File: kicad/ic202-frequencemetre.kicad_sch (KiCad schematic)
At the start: 36 parts, among them J1 +12V IN, J2 RF IN, J3 DIV SEL, Q1 2N2369, U1 L7805, U2 LM317L, U3 MB506

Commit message: Modification 1 : rail 3 V et afficheur LCD TN au bout d'une nappe
La fiche docs/LCD.png montre un afficheur a cristaux liquides TN multiplexe
en 1/4 duty et 1/2 bias sous 3,0 V, et non un afficheur a LED. Consequences :

- rail regule ramene de 3,3 V a 3,0 V, R2 passe de 160 R a 140 R ;
- les 10 broches se repartissent en 4 communs et 6 segments ;
- les resistances de limitation disparaissent au profit d'une polarisation a
  mi-tension : R7..R16 de 100 k vers VLCD_MID, pont R17/R18 et decouplage C12.
  Une broche en haute impedance fournit ainsi le troisieme niveau ;
- J4 represente le connecteur de la nappe 10 conducteurs vers le LCD deporte.

L'ancien symbole 7SEG_3DIGIT_CC est remplace par LCD_3DIGIT_TN_10PIN. La
repartition COM/SEG sur les 10 broches reste une hypothese, signalee dans le
README et a confirmer avant fabrication.

ERC sans erreur ni avertissement, netlist verifiee broche a broche.

Co-Authored-By: Claude Opus 5 <noreply@anthropic.com>
Claude-Session: https://claude.ai/code/session_017jkpXZgM5sH1vt8JFfAijf
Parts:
- removed DS1: 3 digit CC, symbol IC202:7SEG_3DIGIT_CC
- added C12: 1u, Capacitor_SMD:C_0805_2012Metric, symbol Device:C
- added DS1: LCD 3 digits TN, symbol IC202:LCD_3DIGIT_TN_10PIN
- added J4: LCD, Connector_JST:JST_SH_SM10B-SRSS-TB_1x10-1MP_P1.00mm_Horizontal, symbol Connector_Generic:Conn_01x10
- added R17, R18: 10k, Resistor_SMD:R_0603_1608Metric, symbol Device:R
- R10, R11, R12, R13, R7, R8, R9: value 220R -> 100k
- R14, R15, R16: value 100R -> 100k
- R2: value 160R -> 140R
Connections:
- net GND: now also C12.2, R18.2
- net LCD_SEG2: now reaches R12.1
- net LCD_SEG2: now also A1.11 (D8), DS1.6 (SEG2), J4.6 (Pin_6)
- net VLCD_MID: now reaches R14.2
- net VLCD_MID: now also R10.2, R11.2, R12.2, R13.2, R15.2, R16.2, R7.2, R8.2, R9.2, C12.1, R17.2, R18.1
- net LCD_COM4: now reaches R10.1
- net LCD_COM4: now also A1.9 (D6), DS1.4 (COM4), J4.4 (Pin_4)
- net LCD_SEG3: now reaches R13.1
- net LCD_SEG3: now also A1.12 (D9), DS1.7 (SEG3), J4.7 (Pin_7)
- net LCD_COM3: now reaches R9.1
- net LCD_COM3: now also A1.7 (D4), DS1.3 (COM3), J4.3 (Pin_3)
- net LCD_SEG1: now reaches R11.1
- net LCD_SEG1: now also A1.10 (D7), DS1.5 (SEG1), J4.5 (Pin_5)
- net LCD_COM1: now reaches R7.1
- net LCD_COM1: now also A1.5 (D2), DS1.1 (COM1), J4.1 (Pin_1)
- net LCD_COM2: now reaches R8.1
- net LCD_COM2: now also A1.6 (D3), DS1.2 (COM2), J4.2 (Pin_2)
- net +3V3 renamed +3V
- net +3V: now also R17.1
- net D10 renamed LCD_SEG4
- net LCD_SEG4: now also DS1.8 (SEG4), J4.8 (Pin_8)
- net D11 renamed LCD_SEG5
- net LCD_SEG5: now also DS1.9 (SEG5), J4.9 (Pin_9)
- net D12 renamed LCD_SEG6
- net LCD_SEG6: now also DS1.10 (SEG6), J4.10 (Pin_10)
- removed net D2: A1.5 (D2), R7.2
- removed net D3: A1.6 (D3), R8.2
- removed net D4: A1.7 (D4), R9.2
- removed net D6: A1.9 (D6), R10.2
- removed net D7: A1.10 (D7), R11.2
- removed net D8: A1.11 (D8), R12.2
- removed net D9: A1.12 (D9), R13.2
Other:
- note added: "AFFICHEUR LCD 3 DIGITS TN (1/4 duty, 1/2 bias, 3V)"
- note added: "ALIMENTATION 12V -> 5V -> 3V"
- note added: "ARDUINO PRO MINI (alimente en 3V)"
- note added: "MISE EN FORME 3V -> D5"
- note added: "R17/R18/C12 : reference VLCD_MID = 3V/2. J4 : nappe 10 conducteurs vers le LCD deporte."
- note added: "R7..R16 : polarisation a mi-tension. Broche Arduino en haute impedance = 1,5 V, sinon 0 ou 3 V."
- note removed: "AFFICHEUR 3 DIGITS MULTIPLEXE (cathode commune)"
- note removed: "ALIMENTATION 12V -> 5V -> 3V3"
- note removed: "ARDUINO PRO MINI 3V3 / 8 MHz"
- note removed: "DS1 : numeros de broches a verifier sur la datasheet de l afficheur reel"
- note removed: "MISE EN FORME 3V3 -> D5"
- note removed: "R7..R13 -> segments A..G R14..R16 -> digits DIG1..DIG3"

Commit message: Modification 2 : corrections de valeurs d'apres le schema relu
docs/Schema_propre.jpg, une reprise nettement plus lisible du schema
manuscrit, a permis de corriger plusieurs valeurs mal lues sur la premiere
photo et de completer un composant manquant :

- R1 100R->220R, R2 160R->300R (diviseur du LM317L) ;
- R4 1k->3,3k (base de Q1), R6 1k->470R (collecteur de Q1) ;
- C8 1n->100n (decouplage de la broche ~IN du MB506) ;
- R17/R18 10k->3,3k chacune (pont de polarisation du LCD) ;
- ajout de R19 (2K2), pull-down manquant sur la sortie OUT du MB506,
  visible sur le schema relu et absent de la premiere transcription ;
- suppression de l'ancien R5 (100k base->GND) et du connecteur J3
  (selecteur SW1/SW2), absents du schema relu ; SW1/SW2 marquees non
  connectees, ce qui fixe le rapport de division a 1/256.

Le README documente le tableau des corrections et les deux points restes
ambigus : le brochage exact de U1 (78xx05) et un reseau optionnel visible
pres de la broche 8 du MB506 dont les deux extremites semblent en l'air
sur le dessin.

ERC : 0 erreur, 0 avertissement. Netlist et regles de lisibilite verifiees.

Co-Authored-By: Claude Sonnet 5 <noreply@anthropic.com>
Claude-Session: https://claude.ai/code/session_017jkpXZgM5sH1vt8JFfAijf
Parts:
- removed J3: DIV SEL, Connector_PinHeader_2.54mm:PinHeader_1x03_P2.54mm_Vertical, symbol Connector_Generic:Conn_01x03
- removed R5: 100k, Resistor_SMD:R_0603_1608Metric, symbol Device:R
- added R19: 2K2, Resistor_SMD:R_0603_1608Metric, symbol Device:R
- C8: value 1n -> 100n
- R1: value 100R -> 220R
- R17, R18: value 10k -> 3k3
- R2: value 140R -> 300R
- R4: value 1k -> 3k3
- R6: value 1k -> 470R
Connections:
- net GND: now also R19.2
- net at C10.1, U3.4 (OUT): now also R19.1
- net SW1: no longer names the net of U3.3 (SW1)
- net SW2: no longer names the net of U3.6 (SW2)
- no-connect marks 13 -> 15
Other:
- note added: "PREDIVISEUR MB506 (division fixe 1/256)"
- note added: "SW1/SW2 non connectes (ouverts) : division fixe par 256. Voir README pour reconfigurer."
- note removed: "J3 : SW1/SW2 ouverts = 1/256 ; relies a +5V = 1/64 (voir README)"
- note removed: "PREDIVISEUR MB506 (1/64 - 1/128 - 1/256 selon J3)"
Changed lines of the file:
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@@
 			)
 		)
-		(property "Value" "100R"
+		(property "Value" "220R"
 			(at 162.56 38.1 90)
 			(show_name no)
@@
 			)
 		)
-		(property "Value" "140R"
+		(property "Value" "300R"
 			(at 162.56 50.8 90)
 			(show_name no)
@@
 			)
 		)
-		(property "Value" "1n"
+		(property "Value" "100n"
 			(at 64.77 113.665 0)
 			(show_name no)
@@
 				)
 				(justify right)
+				(hide no)
 			)
 		)
@@
 	)
 	(symbol
-		(lib_id "Connector_Generic:Conn_01x03")
-		(at 55.88 132.08 180)
-		(unit 1)
-		(body_style 1)
-		(exclude_from_sim no)
-		(in_bom yes)
-		(on_board yes)
-		(in_pos_files yes)
-		(dnp no)
-		(property "Reference" "J3"
-			(at 55.88 127.0 0)
-			(show_name no)
-			(do_not_autoplace no)
-			(effects
-				(font
-					(size 1.27 1.27)
-				)
-			)
-		)
-		(property "Value" "DIV SEL"
-			(at 55.88 125.73 0)
-			(show_name no)
-			(do_not_autoplace no)
-			(effects
-				(font
-					(size 1.27 1.27)
-				)
-			)
-		)
-		(property "Footprint" "Connector_PinHeader_2.54mm:PinHeader_1x03_P2.54mm_Vertical"
-			(at 55.88 132.08 0)
-			(hide yes)
-			(show_name no)
-			(do_not_autoplace no)
-			(effects
-				(font
-					(size 1.27 1.27)
-				)
-			)
-		)
-		(property "Datasheet" ""
-			(at 55.88 132.08 0)
-			(hide yes)
-			(show_name no)
-			(do_not_autoplace no)
-			(effects
-				(font
-					(size 1.27 1.27)
-				)
-			)
-		)
-		(property "Description" "Generic connector, single row, 01x03, script generated (kicad-library-utils/schlib/autogen/connector/)"
-			(at 55.88 132.08 0)
-			(hide yes)
-			(show_name no)
-			(do_not_autoplace no)
-			(effects
-				(font
-					(size 1.27 1.27)
-				)
-			)
-		)
-		(pin "1"
-		)
-		(pin "2"
-		)
-		(pin "3"
-		)
-		(instances
-			(project "ic202-frequencemetre"
-				(path "/77e9ff15-8520-461e-95f2-e48831172f30"
-					(reference "J3")
-					(unit 1)
-				)
-			)
-		)
-	)
-	(symbol
 		(lib_id "Device:C")
 		(at 119.38 101.6 90)
@@
 			)
 		)
-		(property "Value" "1k"
+		(property "Value" "3k3"
 			(at 139.7 101.6 270)
 			(show_name no)
@@
 	)
 	(symbol
-		(lib_id "Device:R")
-		(at 154.94 111.76 0)
-		(unit 1)
-		(body_style 1)
-		(exclude_from_sim no)
-		(in_bom yes)
-		(on_board yes)
-		(in_pos_files yes)
-		(dnp no)
-		(property "Reference" "R5"
-			(at 152.4 111.76 90)
-			(show_name no)
-			(do_not_autoplace no)
-			(effects
-				(font
-					(size 1.27 1.27)
-				)
-			)
-		)
-		(property "Value" "100k"
-			(at 154.94 111.76 90)
-			(show_name no)
-			(do_not_autoplace no)
-			(effects
-				(font
-					(size 1.27 1.27)
-				)
-				(hide no)
-			)
-		)
-		(property "Footprint" "Resistor_SMD:R_0603_1608Metric"
-			(at 153.162 111.76 90)
-			(hide yes)
-			(show_name no)
-			(do_not_autoplace no)
-			(effects
-				(font
-					(size 1.27 1.27)
-				)
-			)
-		)
-		(property "Datasheet" ""
-			(at 154.94 111.76 0)
-			(hide yes)
-			(show_name no)
-			(do_not_autoplace no)
-			(effects
-				(font
-					(size 1.27 1.27)
-				)
-			)
-		)
-		(property "Description" "Resistor"
-			(at 154.94 111.76 0)
-			(hide yes)
-			(show_name no)
-			(do_not_autoplace no)
-			(effects
-				(font
-					(size 1.27 1.27)
-				)
-			)
-		)
-		(pin "1"
-		)
-		(pin "2"
-		)
-		(instances
-			(project "ic202-frequencemetre"
-				(path "/77e9ff15-8520-461e-95f2-e48831172f30"
-					(reference "R5")
-					(unit 1)
-				)
-			)
-		)
-	)
-	(symbol
 		(lib_id "Transistor_BJT:Q_NPN_BEC")
 		(at 160.02 101.6 0)
@@
 			)
 		)
-		(property "Value" "1k"
+		(property "Value" "470R"
 			(at 162.56 86.36 90)
 			(show_name no)
@@
 	(wire
 		(pts
-			(xy 99.06 101.60000000000001) (xy 115.57 101.6)
+			(xy 99.06 101.60000000000001) (xy 107.95 101.6)
 		)
 		(stroke
@@
 	(wire
 		(pts
-			(xy 123.19 101.6) (xy 135.89 101.6)
+			(xy 107.95 101.6) (xy 115.57 101.6)
 		)
 		(stroke
@@
 	(wire
 		(pts
-			(xy 143.51 101.6) (xy 154.94 101.6)
+			(xy 123.19 101.6) (xy 135.89 101.6)
 		)
 		(stroke
@@
 	(wire
 		(pts
-			(xy 154.94 101.6) (xy 154.94 107.95)
+			(xy 143.51 101.6) (xy 154.94 101.6)
 		)
 		(stroke
@@
 		)
 	)
-	(junction
-		(at 154.94 101.6)
-		(diameter 0)
-		(color 0 0 0 0)
-	)
 	(wire
 		(pts
@@
 		)
 	)
-	(label "SW1"
-		(at 73.66 109.22000000000001 180)
-		(effects
-			(font
-				(size 1.27 1.27)
-			)
-			(justify right bottom)
-		)
-	)
 	(label "GND"
 		(at 86.36 119.38000000000001 270)
@@
 		)
 	)
-	(label "SW2"
-		(at 73.66 111.76 180)
-		(effects
-			(font
-				(size 1.27 1.27)
-			)
-			(justify right bottom)
-		)
-	)
 	(label "+5V"
 		(at 104.14 123.19 90)
@@
 		)
 	)
-	(label "SW1"
-		(at 60.96 134.62 0)
-		(effects
-			(font
-				(size 1.27 1.27)
-			)
-			(justify left bottom)
-		)
-	)
-	(label "SW2"
-		(at 60.96 132.08 0)
-		(effects
-			(font
-				(size 1.27 1.27)
-			)
-			(justify left bottom)
-		)
-	)
-	(label "+5V"
-		(at 60.96 129.54000000000002 0)
-		(effects
-			(font
-				(size 1.27 1.27)
-			)
-			(justify left bottom)
-		)
-	)
-	(label "GND"
-		(at 154.94 115.57000000000001 270)
-		(effects
-			(font
-				(size 1.27 1.27)
-			)
-			(justify right bottom)
-		)
-	)
 	(label "+3V"
 		(at 162.56 82.55 90)
@@
 		)
 	)
-	(text "PREDIVISEUR MB506  (1/64 - 1/128 - 1/256 selon J3)"
+	(text "PREDIVISEUR MB506  (division fixe 1/256)"
 		(exclude_from_sim no)
 		(at 25.4 83.82 0)
@@
 		)
 	)
-	(text "J3 : SW1/SW2 ouverts = 1/256 ; relies a +5V = 1/64 (voir README)"
+	(text "SW1/SW2 non connectes (ouverts) : division fixe par 256. Voir README pour reconfigurer."
 		(exclude_from_sim no)
 		(at 25.4 142.24 0)
@@
 			)
 		)
-		(property "Value" "10k"
+		(property "Value" "3k3"
 			(at 297.18 208.28 90)
 			(show_name no)
@@
 			)
 		)
-		(property "Value" "10k"
+		(property "Value" "3k3"
 			(at 297.18 220.98 90)
 			(show_name no)
@@
 		)
 	)
+	(symbol
+		(lib_id "Device:R")
+		(at 107.95 109.22 0)
+		(unit 1)
+		(body_style 1)
+		(exclude_from_sim no)
+		(in_bom yes)
+		(on_board yes)
+		(in_pos_files yes)
+		(dnp no)
+		(property "Reference" "R19"
+			(at 105.41 109.22 90)
+			(show_name no)
+			(do_not_autoplace no)
+			(effects
+				(font
+					(size 1.27 1.27)
+				)
+			)
+		)
+		(property "Value" "2K2"
+			(at 107.95 109.22 90)
+			(show_name no)
+			(do_not_autoplace no)
+			(effects
+				(font
+					(size 1.27 1.27)
+				)
+				(hide no)
+			)
+		)
+		(property "Footprint" "Resistor_SMD:R_0603_1608Metric"
+			(at 106.172 109.22 90)
+			(hide yes)
+			(show_name no)
+			(do_not_autoplace no)
+			(effects
+				(font
+					(size 1.27 1.27)
+				)
+			)
+		)
+		(property "Datasheet" ""
+			(at 107.95 109.22 0)
+			(hide yes)
+			(show_name no)
+			(do_not_autoplace no)
+			(effects
+				(font
+					(size 1.27 1.27)
+				)
+			)
+		)
+		(property "Description" "Resistor"
+			(at 107.95 109.22 0)
+			(hide yes)
+			(show_name no)
+			(do_not_autoplace no)
+			(effects
+				(font
+					(size 1.27 1.27)
+				)
+			)
+		)
+		(pin "1"
+		)
+		(pin "2"
+		)
+		(instances
+			(project "ic202-frequencemetre"
+				(path "/77e9ff15-8520-461e-95f2-e48831172f30"
+					(reference "R19")
+					(unit 1)
+				)
+			)
+		)
+	)
+	(wire
+		(pts
+			(xy 107.95 101.6) (xy 107.95 105.41)
+		)
+		(stroke
+			(width 0)
+			(type default)
+		)
+	)
+	(junction
+		(at 107.95 101.6)
+		(diameter 0)
+		(color 0 0 0 0)
+	)
+	(label "GND"
+		(at 107.95 113.03 270)
+		(effects
+			(font
+				(size 1.27 1.27)
+			)
+			(justify right bottom)
+		)
+	)
+	(no_connect
+		(at 73.66 109.22000000000001)
+	)
+	(no_connect
+		(at 73.66 111.76)
+	)
 	(sheet_instances

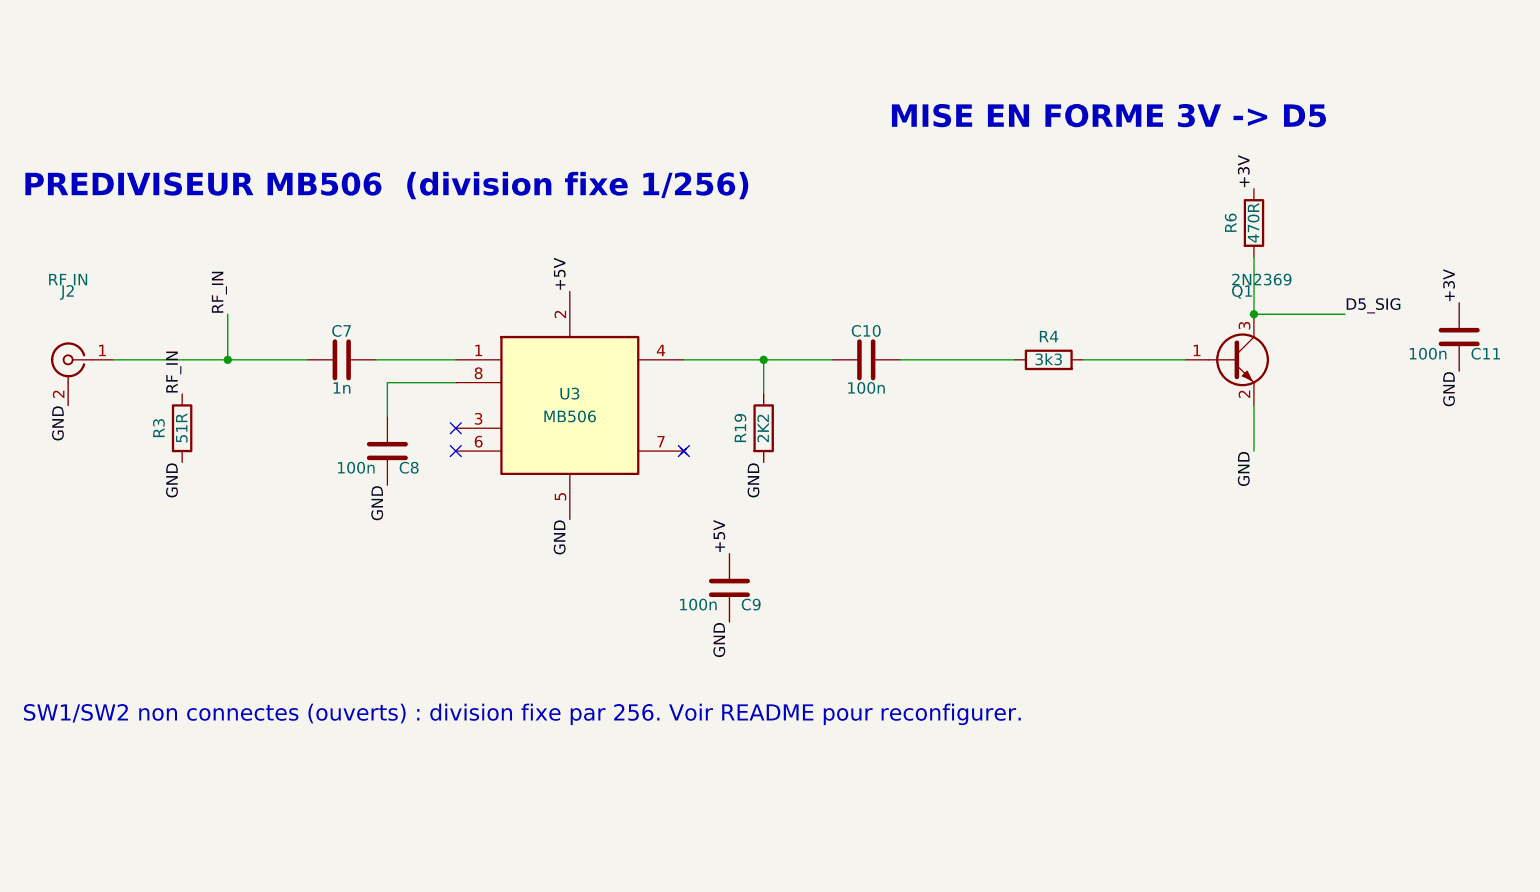
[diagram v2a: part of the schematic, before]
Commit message: Prediviseur MB506 cable en division fixe par 64
SW1 et SW2 (broches 3 et 6) relies au rail +5V (niveau H), au lieu d'etre
laisses flottants. D'apres la table du constructeur, SW1=H et SW2=H donnent
le rapport 1/64.

C8 deplacee de quelques mm pour degager la rangee des broches SW1/SW2 et
eviter que les etiquettes +5V ne chevauchent son corps.

Titre du bloc et note explicative mis a jour en consequence. ERC : 0 erreur,
0 avertissement. Regles de lisibilite verifiees.

Co-Authored-By: Claude Sonnet 5 <noreply@anthropic.com>
Claude-Session: https://claude.ai/code/session_017jkpXZgM5sH1vt8JFfAijf
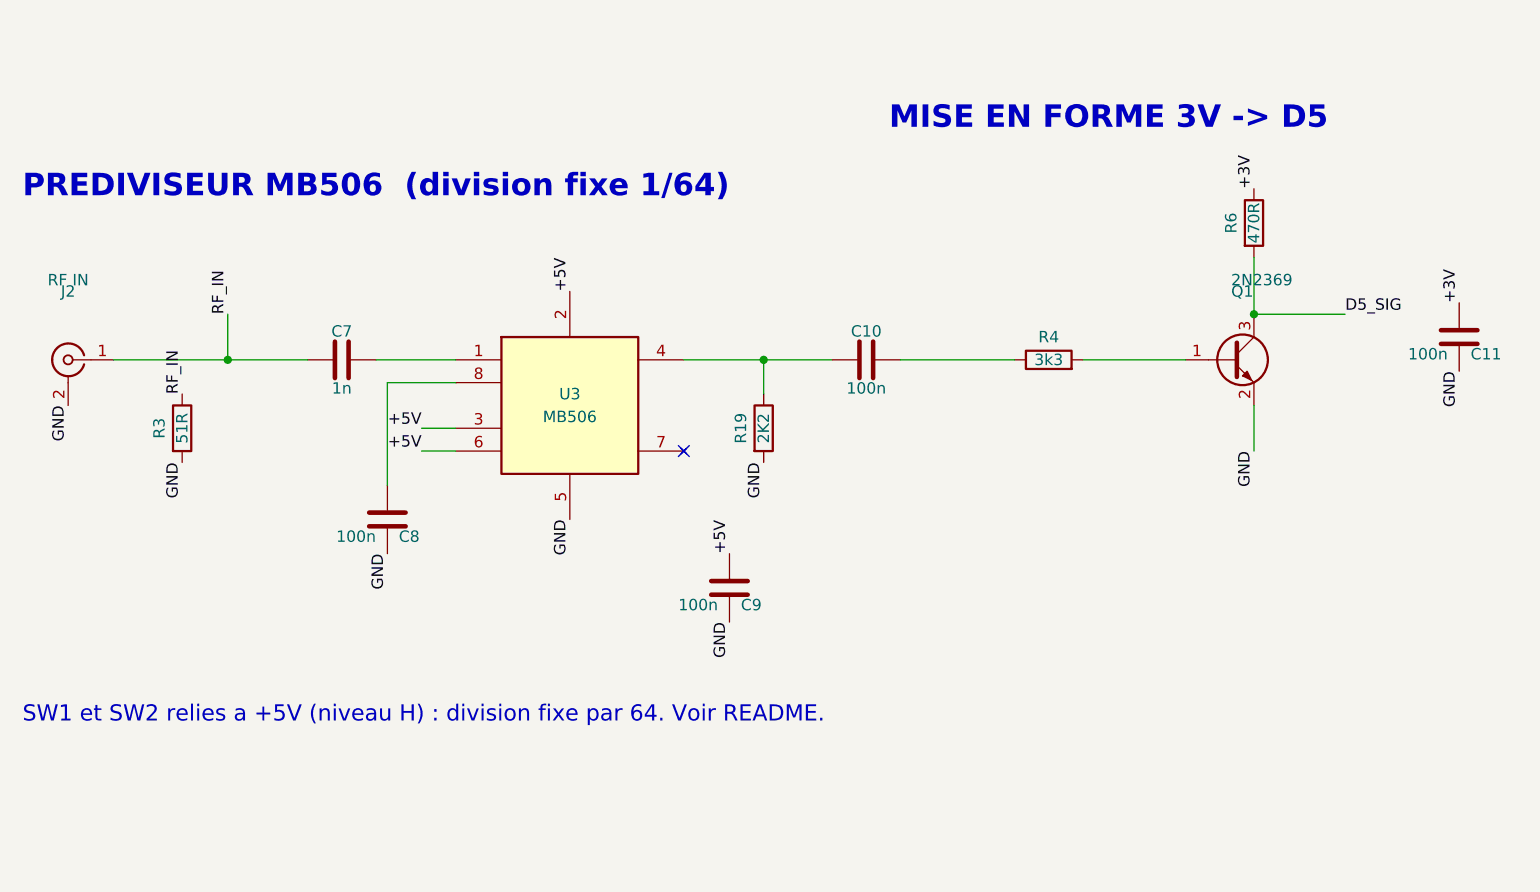
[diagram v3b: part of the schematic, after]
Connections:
- net +5V: now also U3.3 (SW1), U3.6 (SW2)
- no-connect marks 15 -> 13
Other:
- note added: "PREDIVISEUR MB506 (division fixe 1/64)"
- note added: "SW1 et SW2 relies a +5V (niveau H) : division fixe par 64. Voir README."
- note removed: "PREDIVISEUR MB506 (division fixe 1/256)"
- note removed: "SW1/SW2 non connectes (ouverts) : division fixe par 256. Voir README pour reconfigurer."
- moved on the sheet: C8
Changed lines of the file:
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@@
 	(symbol
 		(lib_id "Device:C")
-		(at 66.04 111.76 0)
+		(at 66.04 119.38 0)
 		(unit 1)
 		(body_style 1)
@@
 		(dnp no)
 		(property "Reference" "C8"
-			(at 67.31 113.665 0)
+			(at 67.31 121.285 0)
 			(show_name no)
 			(do_not_autoplace no)
@@
 		)
 		(property "Value" "100n"
-			(at 64.77 113.665 0)
+			(at 64.77 121.285 0)
 			(show_name no)
 			(do_not_autoplace no)
@@
 		)
 		(property "Footprint" "Capacitor_SMD:C_0603_1608Metric"
-			(at 62.23 110.795 0)
+			(at 62.23 118.41499999999999 0)
 			(hide yes)
 			(show_name no)
@@
 		)
 		(property "Datasheet" ""
-			(at 66.04 111.76 0)
+			(at 66.04 119.38 0)
 			(hide yes)
 			(show_name no)
@@
 		)
 		(property "Description" "Unpolarized capacitor"
-			(at 66.04 111.76 0)
+			(at 66.04 119.38 0)
 			(hide yes)
 			(show_name no)
@@
 	(wire
 		(pts
-			(xy 66.04 104.14) (xy 66.04 107.95)
+			(xy 66.04 104.14) (xy 66.04 115.57)
 		)
 		(stroke
@@
 	)
 	(label "GND"
-		(at 66.04 115.57000000000001 270)
+		(at 66.04 123.19 270)
 		(effects
 			(font
@@
 		)
 	)
-	(text "PREDIVISEUR MB506  (division fixe 1/256)"
+	(text "PREDIVISEUR MB506  (division fixe 1/64)"
 		(exclude_from_sim no)
 		(at 25.4 83.82 0)
@@
 		)
 	)
-	(text "SW1/SW2 non connectes (ouverts) : division fixe par 256. Voir README pour reconfigurer."
+	(text "SW1 et SW2 relies a +5V (niveau H) : division fixe par 64. Voir README."
 		(exclude_from_sim no)
 		(at 25.4 142.24 0)
@@
 		)
 	)
-	(no_connect
-		(at 73.66 109.22000000000001)
+	(wire
+		(pts
+			(xy 73.66 109.22000000000001) (xy 69.85 109.22)
+		)
+		(stroke
+			(width 0)
+			(type default)
+		)
 	)
-	(no_connect
-		(at 73.66 111.76)
+	(wire
+		(pts
+			(xy 73.66 111.76) (xy 69.85 111.76)
+		)
+		(stroke
+			(width 0)
+			(type default)
+		)
+	)
+	(label "+5V"
+		(at 69.85 109.22 180)
+		(effects
+			(font
+				(size 1.27 1.27)
+			)
+			(justify right bottom)
+		)
+	)
+	(label "+5V"
+		(at 69.85 111.76 180)
+		(effects
+			(font
+				(size 1.27 1.27)
+			)
+			(justify right bottom)
+		)
 	)
 	(sheet_instances
